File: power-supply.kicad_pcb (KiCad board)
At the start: 2 copper layers, 110 x 95 mm, 62 parts, among them J1 KRE, J10 KRE, J11 Fan, J12 Conn_01x04, J14 I2C, J15 Conn_01x04, J2 Conn_01x05, J3 KRE, J5 Conn_01x20, J7 Conn_01x20, K1 Rele 5V, K2 Rele 5V, Q3 IRF840, Q4 MMBT3904, Q5 MMBT3904, Q6 MMBT3904, U1 LM324, U3 TC4427, U4 AMS1117-5.0

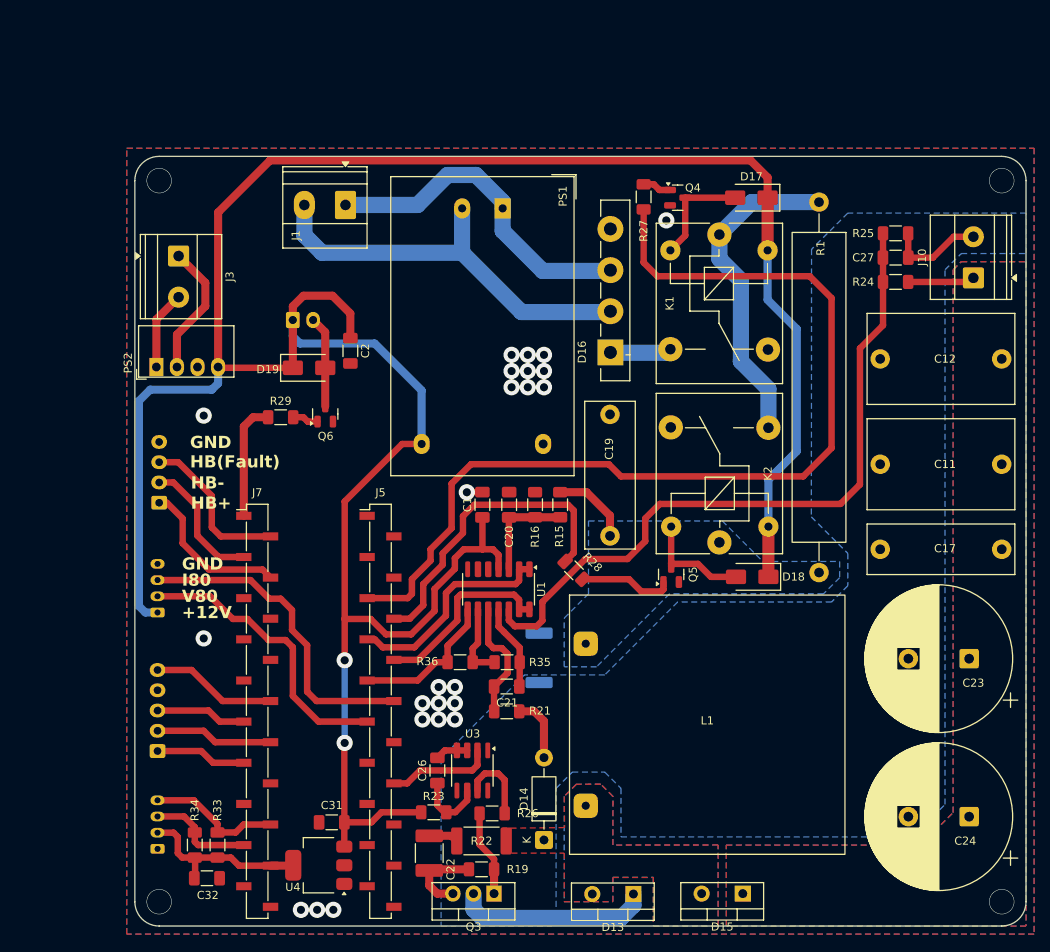
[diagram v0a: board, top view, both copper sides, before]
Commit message: docs: add 3D renders, comprehensive README, CERN-OHL-S license, and update PCB routing
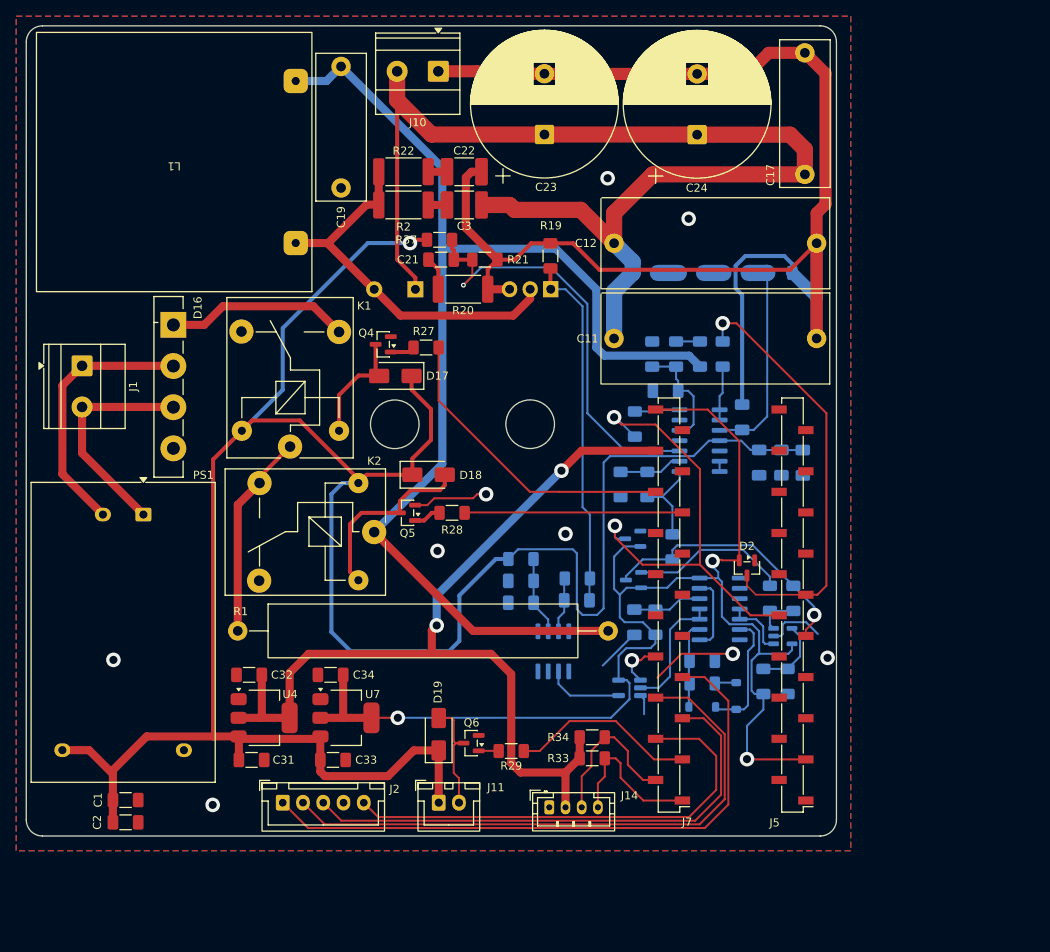
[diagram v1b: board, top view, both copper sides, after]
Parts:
- removed D13: MUR1560, Package_TO_SOT_THT:TO-220-2_Vertical
- removed D14: MUR160, Diode_THT:D_DO-41_SOD81_P10.16mm_Horizontal
- removed J12: Conn_01x04, Connector_JST:JST_XH_B4B-XH-A_1x04_P2.50mm_Vertical
- removed J15: Conn_01x04, Connector_JST:JST_PH_B4B-PH-K_1x04_P2.00mm_Vertical
- removed J3: KRE, TerminalBlock_Phoenix:TerminalBlock_Phoenix_MKDS-1,5-2-5.08_1x02_P5.08mm_Horizontal
- removed PS2: MEE1S1212SC, Converter_DCDC:Converter_DCDC_Murata_MEE1SxxxxSC_THT
- added C28: 100nF, Capacitor_SMD:C_1206_3216Metric_Pad1.33x1.80mm_HandSolder, B.Cu at (169.6, 114.8)
- added C29: 100nF, Capacitor_SMD:C_1206_3216Metric_Pad1.33x1.80mm_HandSolder, B.Cu at (162.7, 115.1)
- added C3: C, Capacitor_SMD:C_1812_4532Metric_Pad1.57x3.40mm_HandSolder, F.Cu at (155.7, 66.0)
- added C33: 10uF, Capacitor_SMD:C_1206_3216Metric_Pad1.33x1.80mm_HandSolder, F.Cu at (139.5, 134.5)
- added C34: 10uF, Capacitor_SMD:C_1206_3216Metric_Pad1.33x1.80mm_HandSolder, F.Cu at (139.2, 124.0)
- added C4: 100nF, Capacitor_SMD:C_1206_3216Metric_Pad1.33x1.80mm_HandSolder, B.Cu at (185.0, 122.3)
- added C5: 100nF, Capacitor_SMD:C_1206_3216Metric_Pad1.33x1.80mm_HandSolder, B.Cu at (176.7, 117.5)
- added C6: 100nF, Capacitor_SMD:C_1206_3216Metric_Pad1.33x1.80mm_HandSolder, B.Cu at (192.1, 97.8)
- added C7: 100nF, Capacitor_SMD:C_1206_3216Metric_Pad1.33x1.80mm_HandSolder, B.Cu at (194.8, 97.8)
- added C8: 100nF, Capacitor_SMD:C_1206_3216Metric_Pad1.33x1.80mm_HandSolder, B.Cu at (197.4, 97.8)
- added D1: BAT54S, Package_TO_SOT_SMD:SOT-23, B.Cu at (176.6, 112.3)
- added D2: BAT54S, Package_TO_SOT_SMD:SOT-23, F.Cu at (190.6, 110.8)
- added D3: BAT54S, Package_TO_SOT_SMD:SOT-23, B.Cu at (176.5, 107.2)
- added D5: 1N4148W, Diode_SMD:D_SOD-123, B.Cu at (189.2, 126.6)
- added D6: 1N4148W, Diode_SMD:D_SOD-123, B.Cu at (185.0, 128.0)
- added R17: 91k, Resistor_SMD:R_1206_3216Metric_Pad1.30x1.75mm_HandSolder, B.Cu at (184.8, 84.4)
- added R2: R, Resistor_SMD:R_2512_6332Metric_Pad1.40x3.35mm_HandSolder, F.Cu at (148.2, 66.0)
- added R3: 20k, Resistor_SMD:R_1206_3216Metric_Pad1.30x1.75mm_HandSolder, B.Cu at (195.6, 124.8)
- added R30: 56k, Resistor_SMD:R_1206_3216Metric_Pad1.30x1.75mm_HandSolder, B.Cu at (183.7, 74.4)
- added R31: 68k, Resistor_SMD:R_1206_3216Metric_Pad1.30x1.75mm_HandSolder, B.Cu at (189.2, 74.4)
- added R37: ~, Resistor_SMD:R_1206_3216Metric_Pad1.30x1.75mm_HandSolder, F.Cu at (152.6, 70.3)
- added R38: 390R, Resistor_SMD:R_1206_3216Metric_Pad1.30x1.75mm_HandSolder, B.Cu at (181.4, 108.2)
- added R39: 390R, Resistor_SMD:R_1206_3216Metric_Pad1.30x1.75mm_HandSolder, B.Cu at (187.6, 84.4)
- added R4: 30k, Resistor_SMD:R_1206_3216Metric_Pad1.30x1.75mm_HandSolder, B.Cu at (192.6, 124.8)
- added R40: 390R, Resistor_SMD:R_1206_3216Metric_Pad1.30x1.75mm_HandSolder, B.Cu at (176.7, 93.0)
- added R5: 10k, Resistor_SMD:R_1206_3216Metric_Pad1.30x1.75mm_HandSolder, B.Cu at (179.3, 117.5)
- added R6: 100k, Resistor_SMD:R_1206_3216Metric_Pad1.30x1.75mm_HandSolder, B.Cu at (185.0, 125.1)
- added R7: 10k, Resistor_SMD:R_1206_3216Metric_Pad1.30x1.75mm_HandSolder, B.Cu at (196.3, 114.6)
- added R8: 10k, Resistor_SMD:R_1206_3216Metric_Pad1.30x1.75mm_HandSolder, B.Cu at (193.4, 114.6)
- added U2: LMV7219M5, Package_TO_SOT_SMD:SOT-23-5, B.Cu at (195.0, 119.2)
- added U5: 74HC00, Package_SO:SOIC-14_3.9x8.7mm_P1.27mm, B.Cu at (187.2, 115.9)
- added U6: 74LVC1G08, Package_TO_SOT_SMD:SOT-23-5_HandSoldering, B.Cu at (176.1, 125.6)
- added U7: AMS1117-3.3, Package_TO_SOT_SMD:SOT-223-3_TabPin2, F.Cu at (141.1, 129.3)
- C11, C12: footprint Capacitor_THT:C_Rect_L18.0mm_W11.0mm_P15.00mm_FKS3_FKP3 -> MyCapacitors:Capacitorzao
- C20, C26, C27, R26, U1, U3: moved to B.Cu
- D15: footprint Package_TO_SOT_THT:TO-220-2_Vertical -> Package_TO_SOT_THT:TO-220-2_Horizontal_TabUp; moved to B.Cu
- J11, J14, J2, R20: moved to F.Cu
- L1: value 1mH -> 2.2 mH
- Q3: value IRF840 -> IRF740; footprint Package_TO_SOT_THT:TO-220-3_Vertical -> Package_TO_SOT_THT:TO-220-3_Horizontal_TabUp; moved to B.Cu
- R15: value XXXX -> 91k; moved to B.Cu
- R16, R25: value XXXX -> 1k5; moved to B.Cu
- R21: value XXXX -> 1k
- R23: value 100R -> 47R; moved to B.Cu
- R24: value XXXX -> 56k; moved to B.Cu
- R35: value XXXX -> 22k; moved to B.Cu
- R36: value R -> 150k; moved to B.Cu
- moved L1 95.7 mm to (119.9, 60.7), turned to 180 degrees
- moved C24 90.6 mm to (184.4, 57.3), turned to 90 degrees
- moved R1 89.2 mm to (127.7, 118.6), turned to 0 degrees
- moved D15 84.8 mm to (149.6, 76.4)
- moved C22 84.2 mm to (155.7, 61.9), turned to 0 degrees
- moved C23 83.3 mm to (165.6, 57.3), turned to 90 degrees
- moved R22 83.2 mm to (148.2, 61.9), turned to 180 degrees
- moved R19 76.2 mm to (166.3, 72.3), turned to 90 degrees
- moved Q3 74.9 mm to (166.3, 76.4)
- moved J10 70.8 mm to (152.5, 49.5), turned to 180 degrees
- moved C2 64.5 mm to (113.9, 142.2), turned to 0 degrees
- moved J11 62.2 mm to (152.5, 139.8)
- moved C17 62.0 mm to (197.7, 47.2), turned to -90 degrees
- moved K1 59.1 mm to (134.2, 95.8), turned to 90 degrees
- moved PS1 58.3 mm to (116.1, 104.2)
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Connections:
- net /PFC/IL_RAW renamed Net-(U1C-+)
- C1 pad 2: GND -> GND_311V
- C11 pad 1: /PFC/GND_350V -> /PFC/GND_380V
- C11 pad 2: /PFC/DC_350V -> /PFC/DC_380V
- C12 pad 1: /PFC/GND_350V -> /PFC/GND_380V
- C12 pad 2: /PFC/DC_350V -> /PFC/DC_380V
- C17 pad 1: /PFC/GND_350V -> /PFC/GND_380V
- C17 pad 2: /PFC/DC_350V -> /PFC/DC_380V
- C19 pad 1: GND -> GND_311V
- C2 pad 2: GND -> GND_311V
- C20 pad 2: GND -> GND_311V
- C21 pad 2: GND -> GND_311V
- C22 pad 2: /PFC/GND_350V -> /PFC/GND_380V
- C23 pad 1: /PFC/DC_350V -> /PFC/DC_380V
- C23 pad 2: /PFC/GND_350V -> /PFC/GND_380V
- C24 pad 1: /PFC/DC_350V -> /PFC/DC_380V
- C24 pad 2: /PFC/GND_350V -> /PFC/GND_380V
- C26 pad 2: GND -> GND_311V
- C27 pad 2: /PFC/GND_350V -> /PFC/GND_380V
- C31 pad 2: GND -> GND_311V
- C32 pad 2: GND -> GND_311V
- D15 pad 1: /PFC/DC_350V -> /PFC/DC_380V
- D16 pad 4: GND -> GND_311V
- J1 pad 1: /L -> /N
- J1 pad 2: /N -> /L
- J10 pad 1: /PFC/DC_350V -> /PFC/GND_380V
- J10 pad 2: /PFC/GND_350V -> /PFC/DC_380V
- J14 pad 1: GND -> GND_311V
- J14 pad 3: /MCU/PB9 -> /MCU/PB13
- J14 pad 4: /MCU/PB8 -> /MCU/PB12
- J2 pad 1: /MCU/PB5 -> /MCU/PA10
- J2 pad 2: /MCU/PB4 -> /MCU/PA9
- J2 pad 3: /MCU/PB3 -> /MCU/PA8
- J2 pad 4: GND -> GND_311V
- J2 pad 5: /MCU/PA15 -> /MCU/PB15
- J5 pad 1: GND -> GND_311V
- J5 pad 2: GND -> GND_311V
- J5 pad 3: unconnected-(J5-Pin_3-Pad3) -> +3V3
- J7 pad 19: GND -> GND_311V
- J7 pad 20: unconnected-(J7-Pin_20-Pad20) -> +3V3
- L1 pad 1: /Low Frequency Rectifier/DC_311V -> /PFC/INDUCTOR_OUT
- L1 pad 2: /PFC/INDUCTOR_OUT -> /Low Frequency Rectifier/DC_311V
- PS1 pad 3: GND -> GND_311V
- Q3 pad 2: Net-(D13-K) -> /PFC/INDUCTOR_OUT
- Q3 pad 3: /PFC/GND_350V -> /PFC/GND_380V
- Q4 pad 2: GND -> GND_311V
- Q5 pad 2: GND -> GND_311V
- Q6 pad 2: GND -> GND_311V
- R15 pad 1: /Low Frequency Rectifier/DC_311V -> Net-(R15-Pad1)
- R16 pad 2: GND -> GND_311V
- R19 pad 2: /PFC/GND_350V -> /PFC/GND_380V
- R20 pad 1: /PFC/GND_350V -> /PFC/GND_380V
- R20 pad 2: GND -> GND_311V
- R21 pad 1: /PFC/GND_350V -> /PFC/GND_380V
- R24 pad 1: /PFC/DC_350V -> /PFC/DC_380V
- R24 pad 2: /PFC/VOUT_RAW -> Net-(R24-Pad2)
- R25 pad 2: /PFC/GND_350V -> /PFC/GND_380V
- R27 pad 2: /MCU/PB11 -> /MCU/PB8
- R28 pad 2: /MCU/PB10 -> /MCU/PB7
- R29 pad 1: /MCU/PB12 -> /MCU/PB14
- R33 pad 2: /MCU/PB8 -> /MCU/PB12
- R34 pad 2: /MCU/PB9 -> /MCU/PB13
- R35 pad 2: GND -> GND_311V
- R36 pad 2: /MCU/PA7 -> Net-(R36-Pad2)
- U1 pad 1: /MCU/PB1 -> Net-(U1A--)
- U1 pad 11: GND -> GND_311V
- U1 pad 12: /PFC/VOUT_RAW -> /PFC/VIN_RAW
- U1 pad 13: /MCU/PB0 -> Net-(U1D--)
- U1 pad 14: /MCU/PB0 -> Net-(U1D--)
- U1 pad 2: /MCU/PB1 -> Net-(U1A--)
- U1 pad 3: /PFC/VIN_RAW -> /PFC/VOUT_RAW
- U1 pad 5: unconnected-(U1B-+-Pad5) -> GND_311V
- U1 pad 6: unconnected-(U1B---Pad6) -> Net-(U1B--)
- U1 pad 7: unconnected-(U1-Pad7) -> Net-(U1B--)
- U1 pad 8: /MCU/PA7 -> Net-(R36-Pad2)
- U3 pad 2: /MCU/PA2 -> Net-(U3-IN_A)
- U3 pad 3: GND -> GND_311V
- U3 pad 4: GND -> GND_311V
- U4 pad 1: GND -> GND_311V
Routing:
- net /PFC/GND_380V: track 0.00 -> 190.8 mm
- net +3V3: track 0.00 -> 160.5 mm, vias 0 -> 3
- net /PFC/DC_380V: track 0.00 -> 144.8 mm
- net /Low Frequency Rectifier/DC_311V: track 9.85 -> 148.5 mm
- net /MCU/PB11: track 121.4 -> 0.00 mm
- net +5V: track 22.2 -> 116.0 mm, vias 0 -> 2
- net /MCU/PA10: track 0.00 -> 77.2 mm
- net /MCU/PA9: track 0.00 -> 72.9 mm
- net /MCU/PA8: track 0.00 -> 64.3 mm
- net /PFC/VOUT_RAW: track 87.4 -> 26.6 mm
- net GND_311V: track 0.00 -> 58.9 mm, vias 0 -> 9
- net /PFC/INDUCTOR_OUT: track 0.00 -> 47.1 mm
- net /MCU/PB15: track 19.4 -> 58.2 mm
- net /MCU/PB10: track 38.6 -> 0.00 mm
- net Net-(U1C-+): track 14.9 -> 53.3 mm, vias 0 -> 1
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- added copper zone on B.Cu, net GND_311V
- added copper zone on F.Cu, net GND_311V
- removed copper zone on B.Cu, net /Low Frequency Rectifier/DC_311V
- removed copper zone on B.Cu, net /PFC/DC_350V
- removed copper zone on F.Cu, net /PFC/DC_350V
- removed copper zone on B.Cu, net /PFC/GND_350V
- removed copper zone on B.Cu, net /PFC/INDUCTOR_OUT
- removed copper zone on F.Cu, net /PFC/INDUCTOR_OUT
- removed copper zone on B.Cu, net GND
- removed copper zone on F.Cu, net GND
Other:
- board size 110 x 95 mm -> 100 x 100 mm
- board text removed: "+12V"
- board text removed: "GND"
- board text removed: "HB(Fault)"
- board text removed: "HB+"
- board text removed: "HB-"
- board text removed: "I80"
- board text removed: "V80"
